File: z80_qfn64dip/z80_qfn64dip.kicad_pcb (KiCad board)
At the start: 4 copper layers, 60 x 23 mm, 38 parts, among them J1 Conn_02x04_Odd_Even, U1 Caravel_QFN, U2 Z80CPU, U3 AZ1117-3.3, U4 AP2112K-1.8, U6 AT25EU0081A

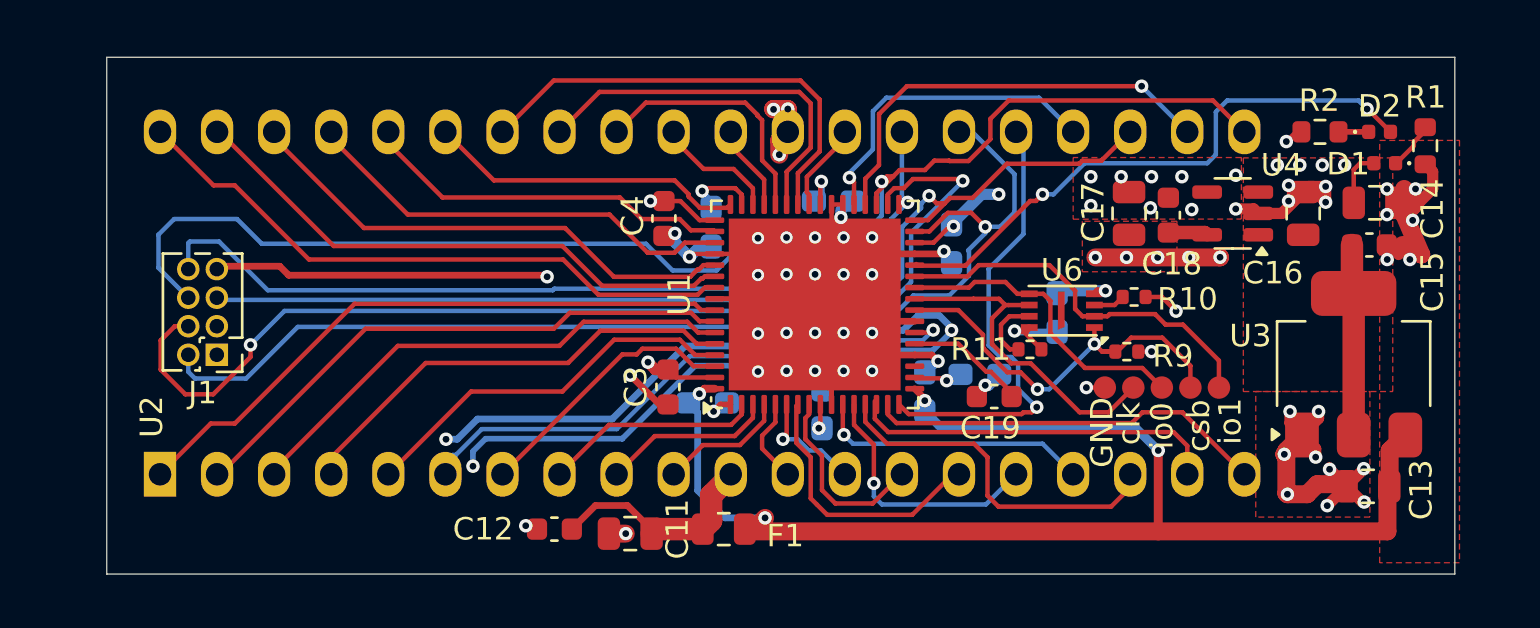
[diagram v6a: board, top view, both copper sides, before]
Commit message: routed and DRC mostly checked
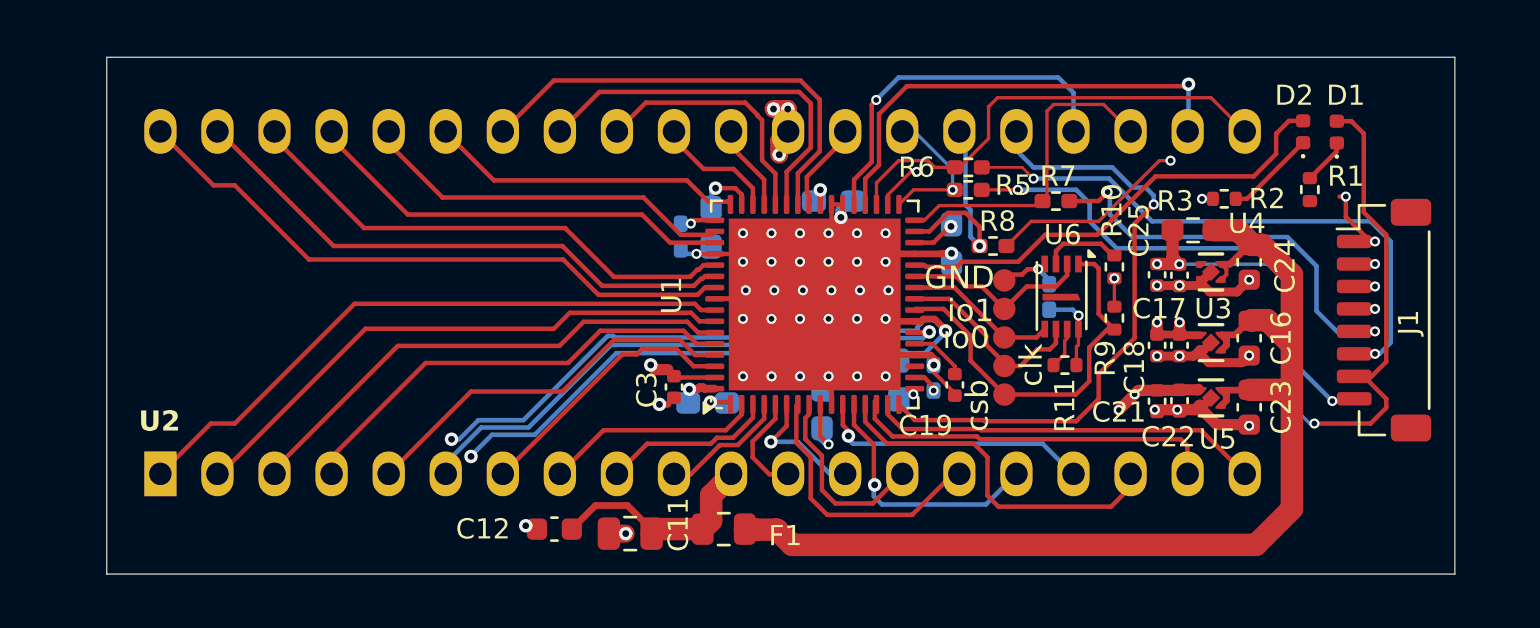
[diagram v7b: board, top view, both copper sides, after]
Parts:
- removed C13: 10uF, Capacitor_SMD:C_0805_2012Metric
- removed C14: 22uF, Capacitor_SMD:C_0805_2012Metric
- removed C15: 100nF, Capacitor_SMD:C_0603_1608Metric
- added C21: 4.7uF, Capacitor_SMD:C_0402_1005Metric, F.Cu at (163.2, 87.8)
- added C22: 100nF, Capacitor_SMD:C_0402_1005Metric, F.Cu at (164.2, 87.8)
- added C23: 4.7uF, Capacitor_SMD:C_0603_1608Metric, F.Cu at (167.3, 88.1)
- added C24: 4.7uF, Capacitor_SMD:C_0603_1608Metric, F.Cu at (167.3, 81.6)
- added C25: 4.7uF, Capacitor_SMD:C_0402_1005Metric, F.Cu at (163.2, 82.2)
- added C26: 100nF, Capacitor_SMD:C_0402_1005Metric, F.Cu at (164.2, 82.2)
- added R3: R0, Resistor_SMD:R_0603_1608Metric_Pad0.98x0.95mm_HandSolder, F.Cu at (164.8, 80.2)
- added R5: 0R, Resistor_SMD:R_0402_1005Metric_Pad0.72x0.64mm_HandSolder, F.Cu at (154.8, 78.4)
- added R6: 0R, Resistor_SMD:R_0402_1005Metric_Pad0.72x0.64mm_HandSolder, F.Cu at (154.9, 77.4)
- added R7: 0R, Resistor_SMD:R_0402_1005Metric_Pad0.72x0.64mm_HandSolder, F.Cu at (158.7, 78.9)
- added R8: 0R, Resistor_SMD:R_0402_1005Metric_Pad0.72x0.64mm_HandSolder, F.Cu at (155.9, 80.9)
- added U5: TPS7A2050PDQNRM3, KiCadModels:DQN0004A-MFG, F.Cu at (165.6, 87.7)
- C16: value 10uF -> 4.7uF; footprint Capacitor_SMD:C_0805_2012Metric -> Capacitor_SMD:C_0603_1608Metric
- C17: value 10uF -> 4.7uF; footprint Capacitor_SMD:C_0805_2012Metric -> Capacitor_SMD:C_0402_1005Metric
- C18, C19, C3: footprint Capacitor_SMD:C_0603_1608Metric -> Capacitor_SMD:C_0402_1005Metric
- C2, C20: footprint Capacitor_SMD:C_0603_1608Metric_Pad1.08x0.95mm_HandSolder -> Capacitor_SMD:C_0402_1005Metric_Pad0.74x0.62mm_HandSolder
- C4: footprint Capacitor_SMD:C_0603_1608Metric -> Capacitor_SMD:C_0402_1005Metric_Pad0.74x0.62mm_HandSolder; moved to B.Cu
- J1: value Conn_02x04_Odd_Even -> Conn_08; footprint Connector_PinHeader_1.27mm:PinHeader_2x04_P1.27mm_Vertical -> Connector_JST:JST_SH_BM08B-SRSS-TB_1x08-1MP_P1.00mm_Vertical
- R1, R2: value 3k3 -> 4k7; footprint Resistor_SMD:R_0603_1608Metric -> Resistor_SMD:R_0402_1005Metric
- U3: value AZ1117-3.3 -> TPS7A2018PDQNRM3; footprint Package_TO_SOT_SMD:SOT-223-3_TabPin2 -> KiCadModels:DQN0004A-MFG
- U4: value AP2112K-1.8 -> TPS7A2033PDQNRM3; footprint Package_TO_SOT_SMD:SOT-23-5 -> KiCadModels:DQN0004A-MFG
- moved J1 52.0 mm to (173.3, 84.2), turned to -90 degrees
- moved TP9 10.2 mm to (156.4, 83.7), turned to 0 degrees
- moved TP12 8.28 mm to (156.5, 87.5), turned to 0 degrees
- moved TP10 7.36 mm to (156.4, 85.0), turned to 0 degrees
- moved TP13 6.54 mm to (156.4, 82.4), turned to 0 degrees
- moved U3 6.42 mm to (165.6, 85.2), turned to 0 degrees
- moved C17 6.29 mm to (164.2, 85.3), turned to -90 degrees
- moved C16 6.05 mm to (167.3, 85.0), turned to -90 degrees
- moved C18 5.82 mm to (163.2, 85.3), turned to -90 degrees
- moved TP11 5.82 mm to (156.5, 86.2), turned to 0 degrees
- moved R1 5.49 mm to (170.0, 78.4)
- moved R2 5.20 mm to (166.2, 78.8)
- moved D2 3.40 mm to (169.7, 75.8), turned to 90 degrees
- moved U4 2.78 mm to (165.6, 82.1), turned to 0 degrees
- moved D1 2.54 mm to (171.2, 75.8), turned to 90 degrees
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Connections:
- C10 pad 2: +5V -> VDDIO
- C16 pad 1: +3V3 -> /VIN_{F}
- C17 pad 1: +1V8 -> VCCD
- C18 pad 1: +1V8 -> VCCD
- C2 pad 1: +1V8 -> VCCD
- C20 pad 1: +3V3 -> VDDA
- C3 pad 2: +1V8 -> VCCD
- C4 pad 1: +1V8 -> VCCD
- C5 pad 2: +5V -> VDDIO
- C6 pad 1: +3V3 -> VDDA
- C7 pad 1: +3V3 -> VDDA
- C8 pad 1: +3V3 -> VDDA
- C9 pad 1: +3V3 -> VDDA
- D1 pad 2: +3V3 -> VDDA
- F1 pad 2: +5V -> /VIN_{F}
- J1 pad 2: HK_JTAG -> Net-(J1-Pin_2)
- J1 pad 5: HK_SDO -> Net-(J1-Pin_5)
- J1 pad 6: HK_SCK -> Net-(J1-Pin_6)
- J1 pad 7: +3V3 -> VDDA
- J1 pad 8: HK_SDI -> Net-(J1-Pin_8)
- R10 pad 2: +3V3 -> VDDA
- R11 pad 2: +3V3 -> VDDA
- R9 pad 1: +3V3 -> VDDA
- U1 pad 17: +5V -> VDDIO
- U1 pad 18: +1V8 -> VCCD
- U1 pad 30: +3V3 -> VDDA
- U1 pad 40: +3V3 -> VDDA
- U1 pad 47: +3V3 -> VDDA
- U1 pad 49: +1V8 -> VCCD
- U1 pad 63: +1V8 -> VCCD
- U1 pad 64: +5V -> VDDIO
- U1 pad 9: +3V3 -> VDDA
- U3 pad 1: GND -> VCCD
- U3 pad 2: +3V3 -> GND
- U3 pad 3: +5V -> /VIN_{F}
- U4 pad 1: +3V3 -> VDDA
- U4 pad 3: +3V3 -> /VIN_{F}
- U4 pad 4: unconnected-(U4-NC-Pad4) -> /VIN_{F}
- U4 pad 5: +1V8 -> GND
- U6 pad 8: +3V3 -> VDDA
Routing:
- net VDDA: track 0.00 -> 79.3 mm, vias 0 -> 9
- net +5V: track 59.7 -> 0.00 mm, vias 4 -> 0
- net /VIN_{F}: track 0.00 -> 51.2 mm
- net +3V3: track 43.5 -> 0.00 mm, vias 13 -> 0
- net VCCD: track 0.00 -> 42.5 mm, vias 0 -> 5
- net HK_JTAG: track 50.3 -> 9.82 mm
- net HK_SCK: track 59.8 -> 20.6 mm, vias 1 -> 0
- net HK_SDI: track 40.9 -> 6.60 mm
- net HK_SDO: track 47.1 -> 14.5 mm, vias 1 -> 0
- net VDDIO: track 0.00 -> 29.6 mm, vias 0 -> 4
- net Net-(J1-Pin_6): track 0.00 -> 25.9 mm, vias 0 -> 2
- net Net-(J1-Pin_8): track 0.00 -> 23.3 mm, vias 0 -> 2
- net HK_CSB: track 48.6 -> 26.3 mm
- net Net-(J1-Pin_2): track 0.00 -> 19.9 mm, vias 0 -> 2
- net Net-(J1-Pin_5): track 0.00 -> 18.0 mm, vias 0 -> 2
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- added copper zone on In2.Cu, net VDDA
- removed copper zone on F.Cu, net +1V8
- removed copper zone on In2.Cu, net +1V8
- removed copper zone on F.Cu, net +3V3
- removed copper zone on In2.Cu, net +3V3
- removed copper zone on F.Cu, net GND

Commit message: add zero-ohm resistor for VDDIO as well, fill B with ground, minor changes
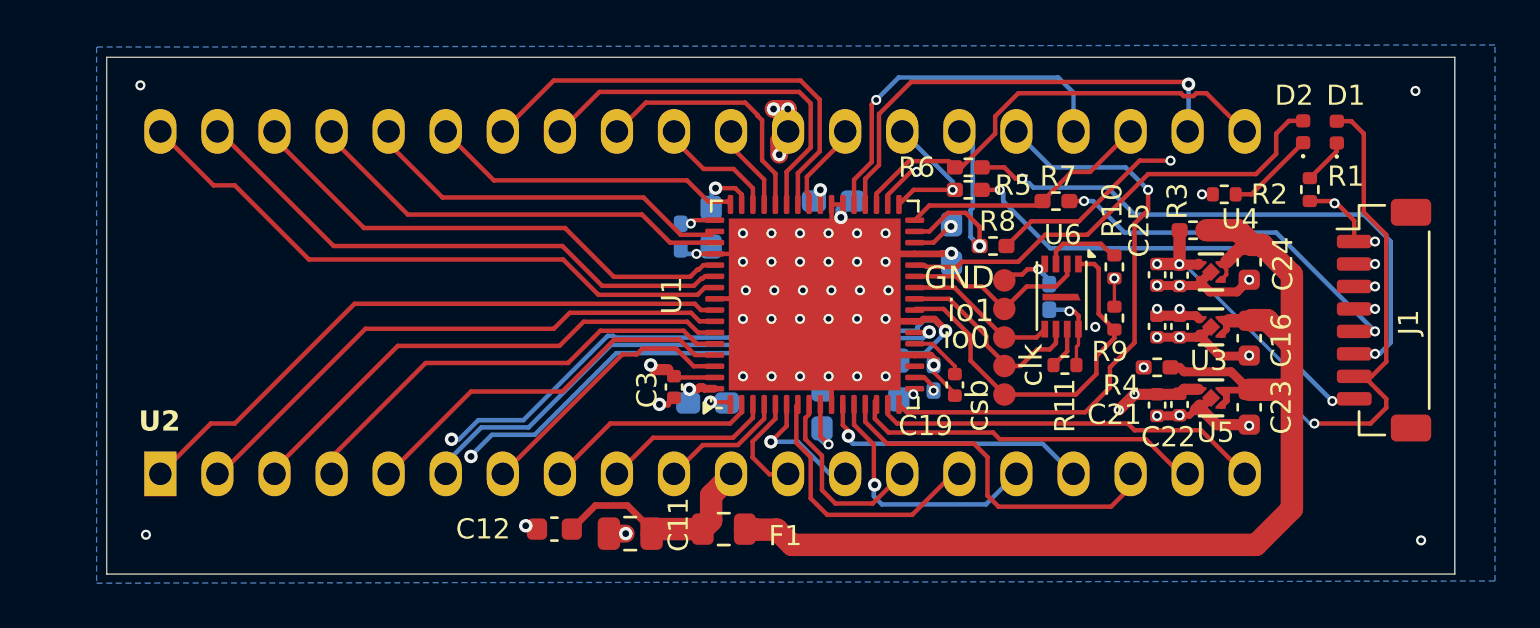
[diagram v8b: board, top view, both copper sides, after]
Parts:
- added R4: 0R, Resistor_SMD:R_0402_1005Metric_Pad0.72x0.64mm_HandSolder, F.Cu at (163.3, 86.3)
- R3: value R0 -> 0R; footprint Resistor_SMD:R_0603_1608Metric_Pad0.98x0.95mm_HandSolder -> Resistor_SMD:R_0402_1005Metric_Pad0.72x0.64mm_HandSolder
- moved C17 0.84 mm to (164.2, 84.5)
- moved C18 0.84 mm to (163.2, 84.5)
- moved U3 0.70 mm to (165.6, 84.5)
- moved R2 0.20 mm to (166.2, 78.6)
- moved C21 0.17 mm to (163.2, 88.0)
- moved C22 0.17 mm to (164.2, 88.0)
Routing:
- net /VIN_{F}: track 51.2 -> 55.2 mm
- net HK_SDO: track 14.5 -> 11.2 mm
- net Net-(J1-Pin_5): track 18.0 -> 16.0 mm
- net VDDA: track 79.3 -> 77.9 mm
- net VDDIO: track 29.6 -> 31.0 mm, vias 4 -> 5
- net /prj_io37: track 27.5 -> 26.5 mm
- net /prj_io35: track 16.5 -> 15.7 mm
- net Net-(J1-Pin_8): track 23.3 -> 22.6 mm
- net GND: track 117.9 -> 118.6 mm, vias 58 -> 63
- added copper zone on B.Cu, net GND
